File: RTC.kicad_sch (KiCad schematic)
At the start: 10 parts, among them U5 PCF8563TS, Y2 MC-306

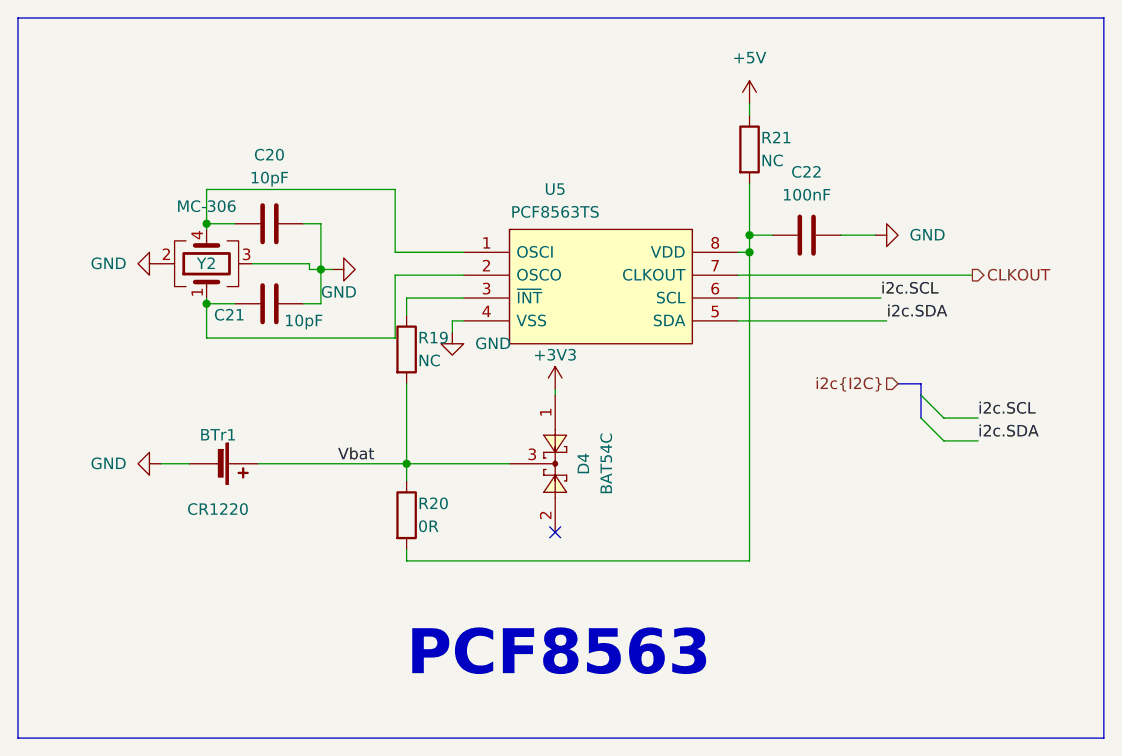
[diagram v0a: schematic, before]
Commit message: Add LORA, SDcard and Volt to 4_20mA scheamtic
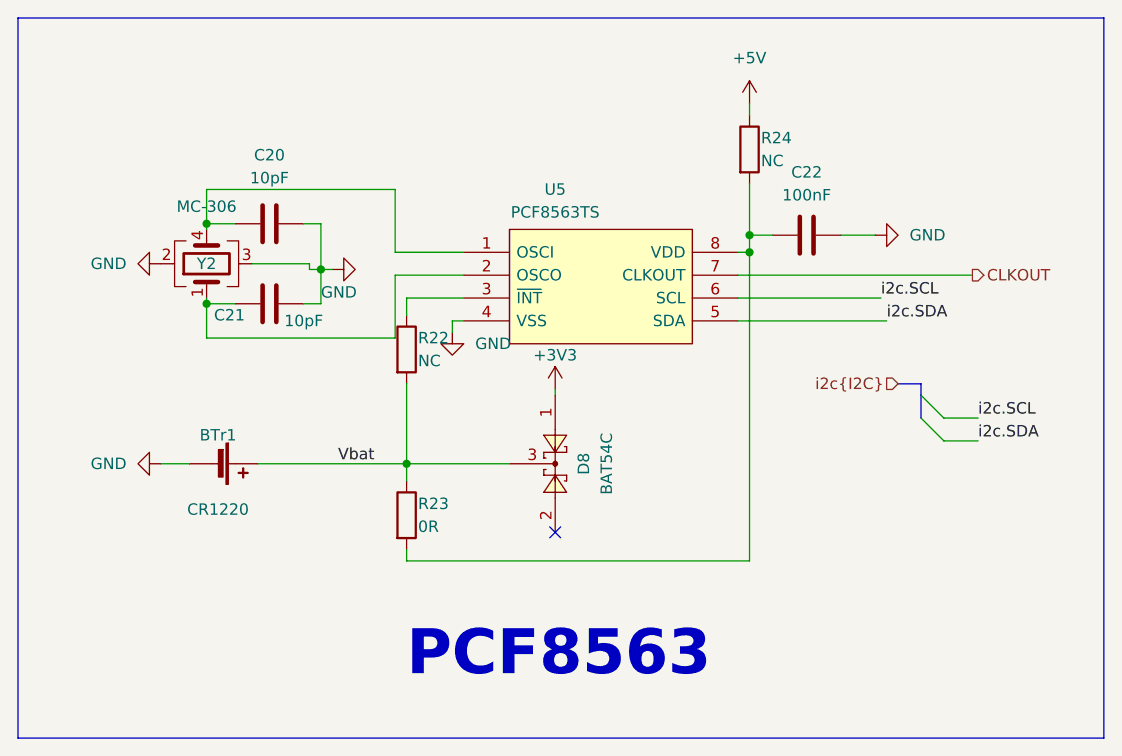
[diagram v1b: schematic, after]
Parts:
- renumbered D4 to D8, R19 to R22, R20 to R23, R21 to R24
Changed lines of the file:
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@@
 		(dnp no)
 		(fields_autoplaced yes)
-		(property "Reference" "#PWR022"
+		(property "Reference" "#PWR034"
 			(at 85.09 65.405 0)
 			(effects
@@
 			(project "DongTamV2"
 				(path "/2303d546-b88a-4ab0-aee1-26e3b32ac9d7/4db09d46-189e-4d6b-adc1-7214f7292c64"
-					(reference "#PWR022")
+					(reference "#PWR034")
 					(unit 1)
 				)
@@
 		(dnp no)
 		(fields_autoplaced yes)
-		(property "Reference" "#PWR019"
+		(property "Reference" "#PWR031"
 			(at 46.355 51.435 0)
 			(effects
@@
 			(project "DongTamV2"
 				(path "/2303d546-b88a-4ab0-aee1-26e3b32ac9d7/4db09d46-189e-4d6b-adc1-7214f7292c64"
-					(reference "#PWR019")
+					(reference "#PWR031")
 					(unit 1)
 				)
@@
 		(on_board yes)
 		(dnp no)
-		(property "Reference" "R21"
+		(property "Reference" "R24"
 			(at 119.38 37.465 0)
 			(effects
@@
 			(project "DongTamV2"
 				(path "/2303d546-b88a-4ab0-aee1-26e3b32ac9d7/4db09d46-189e-4d6b-adc1-7214f7292c64"
-					(reference "R21")
+					(reference "R24")
 					(unit 1)
 				)
@@
 		(dnp no)
 		(fields_autoplaced yes)
-		(property "Reference" "#PWR024"
+		(property "Reference" "#PWR036"
 			(at 118.11 37.465 0)
 			(effects
@@
 			(project "DongTamV2"
 				(path "/2303d546-b88a-4ab0-aee1-26e3b32ac9d7/4db09d46-189e-4d6b-adc1-7214f7292c64"
-					(reference "#PWR024")
+					(reference "#PWR036")
 					(unit 1)
 				)
@@
 		(on_board yes)
 		(dnp no)
-		(property "Reference" "D4"
+		(property "Reference" "D8"
 			(at 99.695 73.66 0)
 			(effects
@@
 			(project "DongTamV2"
 				(path "/2303d546-b88a-4ab0-aee1-26e3b32ac9d7/4db09d46-189e-4d6b-adc1-7214f7292c64"
-					(reference "D4")
+					(reference "D8")
 					(unit 1)
 				)
@@
 		(dnp no)
 		(fields_autoplaced yes)
-		(property "Reference" "#PWR025"
+		(property "Reference" "#PWR037"
 			(at 138.43 48.26 0)
 			(effects
@@
 			(project "DongTamV2"
 				(path "/2303d546-b88a-4ab0-aee1-26e3b32ac9d7/4db09d46-189e-4d6b-adc1-7214f7292c64"
-					(reference "#PWR025")
+					(reference "#PWR037")
 					(unit 1)
 				)
@@
 		(on_board yes)
 		(dnp no)
-		(property "Reference" "#PWR021"
+		(property "Reference" "#PWR033"
 			(at 78.105 52.07 0)
 			(effects
@@
 			(project "DongTamV2"
 				(path "/2303d546-b88a-4ab0-aee1-26e3b32ac9d7/4db09d46-189e-4d6b-adc1-7214f7292c64"
-					(reference "#PWR021")
+					(reference "#PWR033")
 					(unit 1)
 				)
@@
 		(on_board yes)
 		(dnp no)
-		(property "Reference" "#PWR023"
+		(property "Reference" "#PWR035"
 			(at 96.52 69.215 0)
 			(effects
@@
 			(project "DongTamV2"
 				(path "/2303d546-b88a-4ab0-aee1-26e3b32ac9d7/4db09d46-189e-4d6b-adc1-7214f7292c64"
-					(reference "#PWR023")
+					(reference "#PWR035")
 					(unit 1)
 				)
@@
 		(on_board yes)
 		(dnp no)
-		(property "Reference" "R19"
+		(property "Reference" "R22"
 			(at 81.28 59.69 0)
 			(effects
@@
 			(project "DongTamV2"
 				(path "/2303d546-b88a-4ab0-aee1-26e3b32ac9d7/4db09d46-189e-4d6b-adc1-7214f7292c64"
-					(reference "R19")
+					(reference "R22")
 					(unit 1)
 				)
@@
 		(on_board yes)
 		(dnp no)
-		(property "Reference" "R20"
+		(property "Reference" "R23"
 			(at 81.28 78.105 0)
 			(effects
@@
 			(project "DongTamV2"
 				(path "/2303d546-b88a-4ab0-aee1-26e3b32ac9d7/4db09d46-189e-4d6b-adc1-7214f7292c64"
-					(reference "R20")
+					(reference "R23")
 					(unit 1)
 				)
@@
 		(dnp no)
 		(fields_autoplaced yes)
-		(property "Reference" "#PWR020"
+		(property "Reference" "#PWR032"
 			(at 46.355 73.66 0)
 			(effects
@@
 			(project "DongTamV2"
 				(path "/2303d546-b88a-4ab0-aee1-26e3b32ac9d7/4db09d46-189e-4d6b-adc1-7214f7292c64"
-					(reference "#PWR020")
-					(unit 1)
-				)
+					(reference "#PWR032")
+					(unit 1)
+				)

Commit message: Feat: Components's layout
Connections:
- net at C21.1, U5.2 (OSCO): now also Y2.4; no longer Y2.1
- net at C20.1, U5.1 (OSCI): now also Y2.1; no longer Y2.4
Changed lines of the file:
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@@
+	(wire
+		(pts
+			(xy 51.435 51.435) (xy 52.705 51.435)
+		)
+		(stroke
+			(width 0)
+			(type default)
+		)
+	)
 	(wire
 		(pts
@@
 	(symbol
 		(lib_id "power:GND")
-		(at 52.705 51.435 270)
+		(at 51.435 51.435 270)
 		(unit 1)
 		(exclude_from_sim no)
@@
 		(fields_autoplaced yes)
 		(property "Reference" "#PWR031"
-			(at 46.355 51.435 0)
+			(at 45.085 51.435 0)
 			(effects
 				(font
@@
 		)
 		(property "Value" "GND"
-			(at 48.895 51.4349 90)
+			(at 47.625 51.4349 90)
 			(effects
 				(font
@@
 		)
 		(property "Footprint" ""
-			(at 52.705 51.435 0)
+			(at 51.435 51.435 0)
 			(effects
 				(font
@@
 		)
 		(property "Datasheet" ""
-			(at 52.705 51.435 0)
+			(at 51.435 51.435 0)
 			(effects
 				(font
@@
 		)
 		(property "Description" ""
-			(at 52.705 51.435 0)
+			(at 51.435 51.435 0)
 			(effects
 				(font
@@
 	)
 	(symbol
+		(lib_id "Device:Crystal_GND23")
+		(at 57.785 51.435 270)
+		(unit 1)
+		(exclude_from_sim no)
+		(in_bom yes)
+		(on_board yes)
+		(dnp no)
+		(property "Reference" "Y2"
+			(at 57.785 51.435 90)
+			(effects
+				(font
+					(size 1.27 1.27)
+				)
+			)
+		)
+		(property "Value" "MC-306"
+			(at 57.785 57.785 90)
+			(effects
+				(font
+					(size 1.27 1.27)
+				)
+			)
+		)
+		(property "Footprint" "Crystal:Crystal_SMD_SeikoEpson_MC306-4Pin_8.0x3.2mm"
+			(at 57.785 51.435 0)
+			(effects
+				(font
+					(size 1.27 1.27)
+				)
+				(hide yes)
+			)
+		)
+		(property "Datasheet" "~"
+			(at 57.785 51.435 0)
+			(effects
+				(font
+					(size 1.27 1.27)
+				)
+				(hide yes)
+			)
+		)
+		(property "Description" ""
+			(at 57.785 51.435 0)
+			(effects
+				(font
+					(size 1.27 1.27)
+				)
+				(hide yes)
+			)
+		)
+		(pin "1"
+		)
+		(pin "2"
+		)
+		(pin "3"
+		)
+		(pin "4"
+		)
+		(instances
+			(project "DongTamV2"
+				(path "/2303d546-b88a-4ab0-aee1-26e3b32ac9d7/4db09d46-189e-4d6b-adc1-7214f7292c64"
+					(reference "Y2")
+					(unit 1)
+				)
+			)
+		)
+	)
+	(symbol
 		(lib_id "Device:R")
 		(at 80.01 79.375 0)
@@
 					(unit 1)
 				)
-			)
-		)
-	)
-	(symbol
-		(lib_id "Device:Crystal_GND23")
-		(at 57.785 51.435 90)
-		(unit 1)
-		(exclude_from_sim no)
-		(in_bom yes)
-		(on_board yes)
-		(dnp no)
-		(property "Reference" "Y2"
-			(at 57.785 51.435 90)
-			(effects
-				(font
-					(size 1.27 1.27)
-				)
-			)
-		)
-		(property "Value" "MC-306"
-			(at 57.785 45.085 90)
-			(effects
-				(font
-					(size 1.27 1.27)
-				)
-			)
-		)
-		(property "Footprint" "Crystal:Crystal_SMD_SeikoEpson_MC306-4Pin_8.0x3.2mm"
-			(at 57.785 51.435 0)
-			(effects
-				(font
-					(size 1.27 1.27)
-				)
-				(hide yes)
-			)
-		)
-		(property "Datasheet" "~"
-			(at 57.785 51.435 0)
-			(effects
-				(font
-					(size 1.27 1.27)
-				)
-				(hide yes)
-			)
-		)
-		(property "Description" ""
-			(at 57.785 51.435 0)
-			(effects
-				(font
-					(size 1.27 1.27)
-				)
-				(hide yes)
-			)
-		)
-		(pin "1"
-		)
-		(pin "2"
-		)
-		(pin "3"
-		)
-		(pin "4"
-		)
-		(instances
-			(project "DongTamV2"
-				(path "/2303d546-b88a-4ab0-aee1-26e3b32ac9d7/4db09d46-189e-4d6b-adc1-7214f7292c64"
-					(reference "Y2")
-					(unit 1)
-				)
-			)
-			(project "dongtam"
-				(path "/6833aec4-3d1d-4261-9b3e-f0452b565dd3/a9a99304-d65b-4ed1-854e-7f464f20419d"
-					(reference "Y?")
-					(unit 1)
-				)

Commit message: layout p1
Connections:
- net +3V3 renamed +3.3V
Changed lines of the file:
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@@
+	)
+	(symbol
+		(lib_id "power:+3.3V")
+		(at 96.52 65.405 0)
+		(unit 1)
+		(exclude_from_sim no)
+		(in_bom yes)
+		(on_board yes)
+		(dnp no)
+		(fields_autoplaced yes)
+		(property "Reference" "#PWR029"
+			(at 96.52 69.215 0)
+			(effects
+				(font
+					(size 1.27 1.27)
+				)
+				(hide yes)
+			)
+		)
+		(property "Value" "+3.3V"
+			(at 96.52 60.325 0)
+			(effects
+				(font
+					(size 1.27 1.27)
+				)
+			)
+		)
+		(property "Footprint" ""
+			(at 96.52 65.405 0)
+			(effects
+				(font
+					(size 1.27 1.27)
+				)
+				(hide yes)
+			)
+		)
+		(property "Datasheet" ""
+			(at 96.52 65.405 0)
+			(effects
+				(font
+					(size 1.27 1.27)
+				)
+				(hide yes)
+			)
+		)
+		(property "Description" "Power symbol creates a global label with name \"+3.3V\""
+			(at 96.52 65.405 0)
+			(effects
+				(font
+					(size 1.27 1.27)
+				)
+				(hide yes)
+			)
+		)
+		(pin "1"
+		)
+		(instances
+			(project "DongTamV2"
+				(path "/2303d546-b88a-4ab0-aee1-26e3b32ac9d7/4db09d46-189e-4d6b-adc1-7214f7292c64"
+					(reference "#PWR029")
+					(unit 1)
+				)
+			)
+		)
 	)
 	(symbol
@@
 					(unit 1)
 				)
-			)
-			(project "dongtam"
-				(path "/6833aec4-3d1d-4261-9b3e-f0452b565dd3/a9a99304-d65b-4ed1-854e-7f464f20419d"
-					(reference "#PWR?")
-					(unit 1)
-				)
-			)
-		)
-	)
-	(symbol
-		(lib_id "power:+3V3")
-		(at 96.52 65.405 0)
-		(unit 1)
-		(exclude_from_sim no)
-		(in_bom yes)
-		(on_board yes)
-		(dnp no)
-		(property "Reference" "#PWR035"
-			(at 96.52 69.215 0)
-			(effects
-				(font
-					(size 1.27 1.27)
-				)
-				(hide yes)
-			)
-		)
-		(property "Value" "+3V3"
-			(at 96.52 61.595 0)
-			(effects
-				(font
-					(size 1.27 1.27)
-				)
-			)
-		)
-		(property "Footprint" ""
-			(at 96.52 65.405 0)
-			(effects
-				(font
-					(size 1.27 1.27)
-				)
-				(hide yes)
-			)
-		)
-		(property "Datasheet" ""
-			(at 96.52 65.405 0)
-			(effects
-				(font
-					(size 1.27 1.27)
-				)
-				(hide yes)
-			)
-		)
-		(property "Description" ""
-			(at 96.52 65.405 0)
-			(effects
-				(font
-					(size 1.27 1.27)
-				)
-				(hide yes)
-			)
-		)
-		(pin "1"
-		)
-		(instances
-			(project "DongTamV2"
-				(path "/2303d546-b88a-4ab0-aee1-26e3b32ac9d7/4db09d46-189e-4d6b-adc1-7214f7292c64"
-					(reference "#PWR035")
-					(unit 1)
-				)
